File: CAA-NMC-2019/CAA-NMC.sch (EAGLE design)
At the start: 28 parts, among them IC1 ATTINY85-20SU, J1 M20-9980346

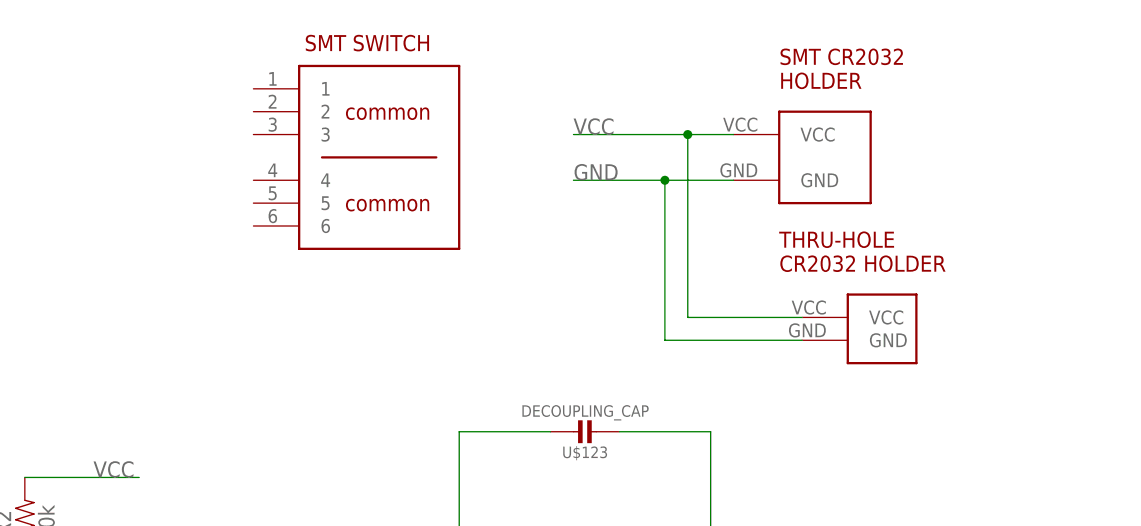
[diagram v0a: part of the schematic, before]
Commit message: fixed battery orientation
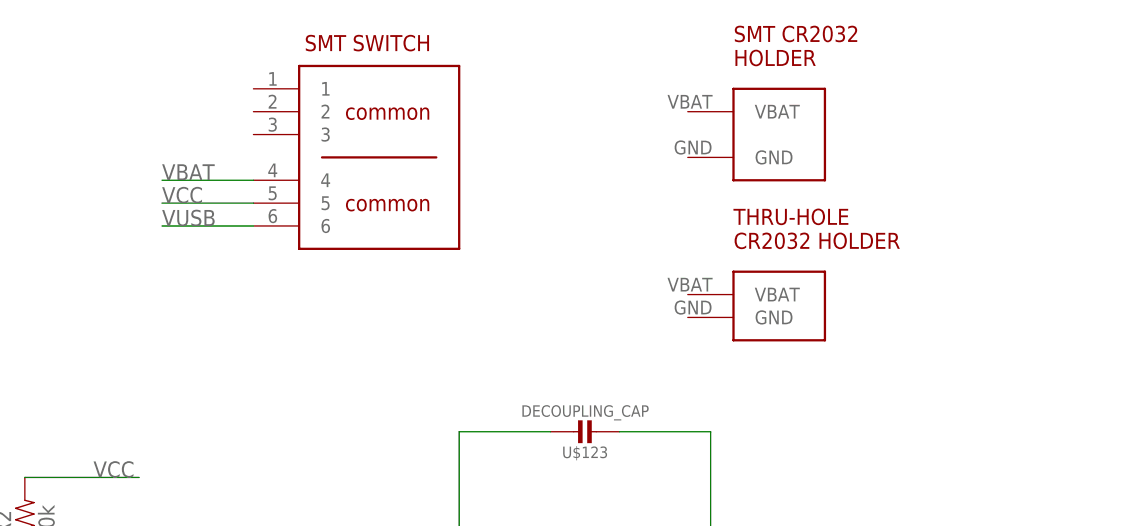
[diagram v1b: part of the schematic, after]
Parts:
- removed U$144: SMT-BATTERY-HOLDER, BadgeParts:SMT-BATTERY-HOLDER
- added U$3: THRU-CR-HOLDER, BadgeParts:THRU-CR-HOLDER
- U$2: value THRU-CR-HOLDER -> SMT-BATTERY-HOLDER; device BadgeParts:THRU-CR-HOLDER -> BadgeParts:SMT-BATTERY-HOLDER
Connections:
- new net VBAT: U$145.4
- new net VUSB: U$145.6
- net GND: no longer U$144.GND, U$2.GND
- net VCC: now also U$145.5; no longer U$144.VCC, U$2.VCC
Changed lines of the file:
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@@
 <part name="U$126" library="BadgeParts" deviceset="RESISTOR" device=""/>
 <part name="U$127" library="BadgeParts" deviceset="RESISTOR" device=""/>
-<part name="U$144" library="BadgeParts" deviceset="SMT-BATTERY-HOLDER" device=""/>
 <part name="U$145" library="BadgeParts" deviceset="SMT-SWITCH" device=""/>
 <part name="U$1" library="BadgeParts" deviceset="PROTO" device=""/>
-<part name="U$2" library="BadgeParts" deviceset="THRU-CR-HOLDER" device=""/>
 <part name="LED1" library="SparkFun-LED" library_urn="urn:adsk.eagle:library:529" deviceset="WS2812B" device="" package3d_urn="urn:adsk.eagle:package:39369/1" value="WS2812B"/>
 <part name="SUPPLY5" library="SparkFun-PowerSymbols" library_urn="urn:adsk.eagle:library:530" deviceset="VDD" device=""/>
@@
 <part name="R1" library="SparkFun-Resistors" library_urn="urn:adsk.eagle:library:532" deviceset="470OHM" device="-0603-1/10W-1%" package3d_urn="urn:adsk.eagle:package:39650/1" value="470"/>
 <part name="R2" library="SparkFun-Resistors" library_urn="urn:adsk.eagle:library:532" deviceset="10KOHM" device="-0603-1/10W-1%" package3d_urn="urn:adsk.eagle:package:39650/1" value="10k"/>
+<part name="U$2" library="BadgeParts" deviceset="SMT-BATTERY-HOLDER" device=""/>
+<part name="U$3" library="BadgeParts" deviceset="THRU-CR-HOLDER" device=""/>
 </parts>
 <sheets>
@@
 <attribute name="VALUE" x="-147.32" y="61.976" size="1.778" layer="96" font="vector" align="top-center"/>
 </instance>
-<instance part="U$144" gate="G$1" x="-127" y="124.46" smashed="yes"/>
 <instance part="U$145" gate="G$1" x="-180.34" y="129.54" smashed="yes"/>
 <instance part="U$1" gate="G$1" x="-63.5" y="101.6" smashed="yes"/>
-<instance part="U$2" gate="G$1" x="-119.38" y="104.14" smashed="yes"/>
 <instance part="LED1" gate="G$1" x="-284.48" y="116.84" smashed="yes">
 <attribute name="NAME" x="-297.18" y="125.222" size="1.778" layer="95"/>
@@
 <attribute name="VALUE" x="-209.296" y="81.28" size="1.778" layer="96" font="vector" rot="R90" align="top-center"/>
 </instance>
+<instance part="U$2" gate="G$1" x="-132.08" y="127" smashed="yes"/>
+<instance part="U$3" gate="G$1" x="-132.08" y="106.68" smashed="yes"/>
 </instances>
 <busses>
@@
 </segment>
 <segment>
-<pinref part="U$144" gate="G$1" pin="VCC"/>
-<wire x1="-132.08" y1="124.46" x2="-137.16" y2="124.46" width="0.1524" layer="91"/>
-<label x="-149.86" y="124.46" size="1.778" layer="95"/>
-<pinref part="U$2" gate="G$1" pin="VCC"/>
-<wire x1="-137.16" y1="124.46" x2="-149.86" y2="124.46" width="0.1524" layer="91"/>
-<wire x1="-124.46" y1="104.14" x2="-137.16" y2="104.14" width="0.1524" layer="91"/>
-<wire x1="-137.16" y1="104.14" x2="-137.16" y2="124.46" width="0.1524" layer="91"/>
-<junction x="-137.16" y="124.46"/>
-</segment>
-<segment>
 <pinref part="U$1" gate="G$1" pin="VCC"/>
 <wire x1="-68.58" y1="101.6" x2="-86.36" y2="101.6" width="0.1524" layer="91"/>
@@
 <wire x1="-210.82" y1="86.36" x2="-198.12" y2="86.36" width="0.1524" layer="91"/>
 <label x="-203.2" y="86.36" size="1.778" layer="95"/>
+</segment>
+<segment>
+<wire x1="-185.42" y1="116.84" x2="-195.58" y2="116.84" width="0.1524" layer="91"/>
+<pinref part="U$145" gate="G$1" pin="5"/>
+<label x="-195.58" y="116.84" size="1.778" layer="95"/>
 </segment>
 </net>
@@
 <wire x1="-5.08" y1="33.02" x2="-5.08" y2="40.64" width="0.1524" layer="91"/>
 <label x="-7.62" y="40.64" size="1.778" layer="95"/>
-</segment>
-<segment>
-<pinref part="U$144" gate="G$1" pin="GND"/>
-<wire x1="-132.08" y1="119.38" x2="-139.7" y2="119.38" width="0.1524" layer="91"/>
-<label x="-149.86" y="119.38" size="1.778" layer="95"/>
-<pinref part="U$2" gate="G$1" pin="GND"/>
-<wire x1="-139.7" y1="119.38" x2="-149.86" y2="119.38" width="0.1524" layer="91"/>
-<wire x1="-124.46" y1="101.6" x2="-139.7" y2="101.6" width="0.1524" layer="91"/>
-<wire x1="-139.7" y1="101.6" x2="-139.7" y2="119.38" width="0.1524" layer="91"/>
-<junction x="-139.7" y="119.38"/>
 </segment>
 <segment>
@@
 </segment>
 </net>
+<net name="VBAT" class="0">
+<segment>
+<wire x1="-185.42" y1="119.38" x2="-195.58" y2="119.38" width="0.1524" layer="91"/>
+<pinref part="U$145" gate="G$1" pin="4"/>
+<label x="-195.58" y="119.38" size="1.778" layer="95"/>
+</segment>
+</net>
+<net name="VUSB" class="0">
+<segment>
+<wire x1="-185.42" y1="114.3" x2="-195.58" y2="114.3" width="0.1524" layer="91"/>
+<pinref part="U$145" gate="G$1" pin="6"/>
+<label x="-195.58" y="114.3" size="1.778" layer="95"/>
+</segment>
+</net>

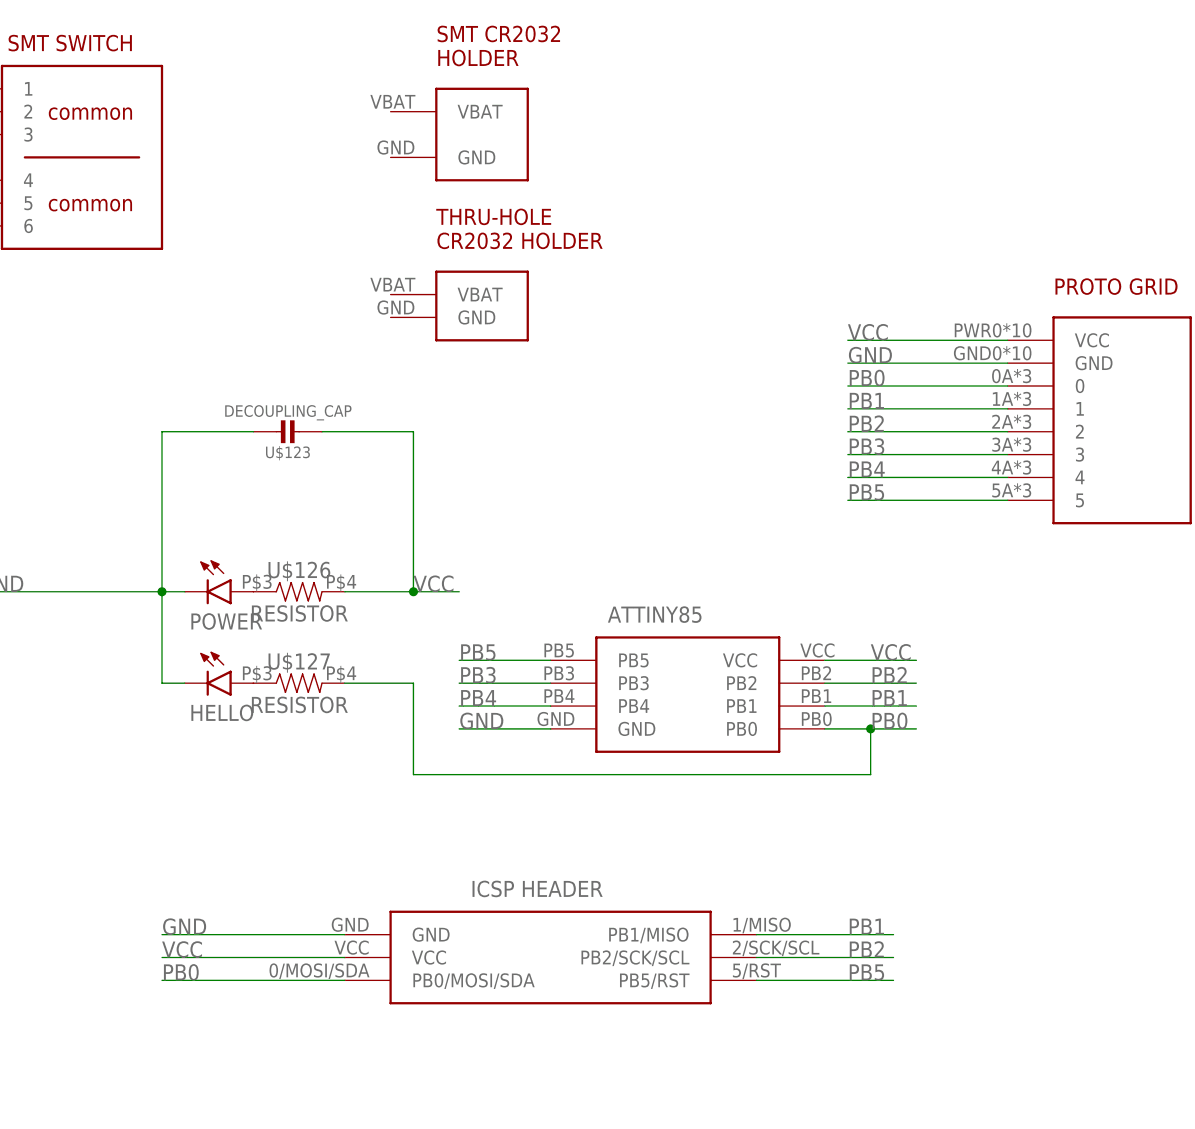
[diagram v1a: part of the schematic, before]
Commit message: Isolated battery/USB power supplies at switch
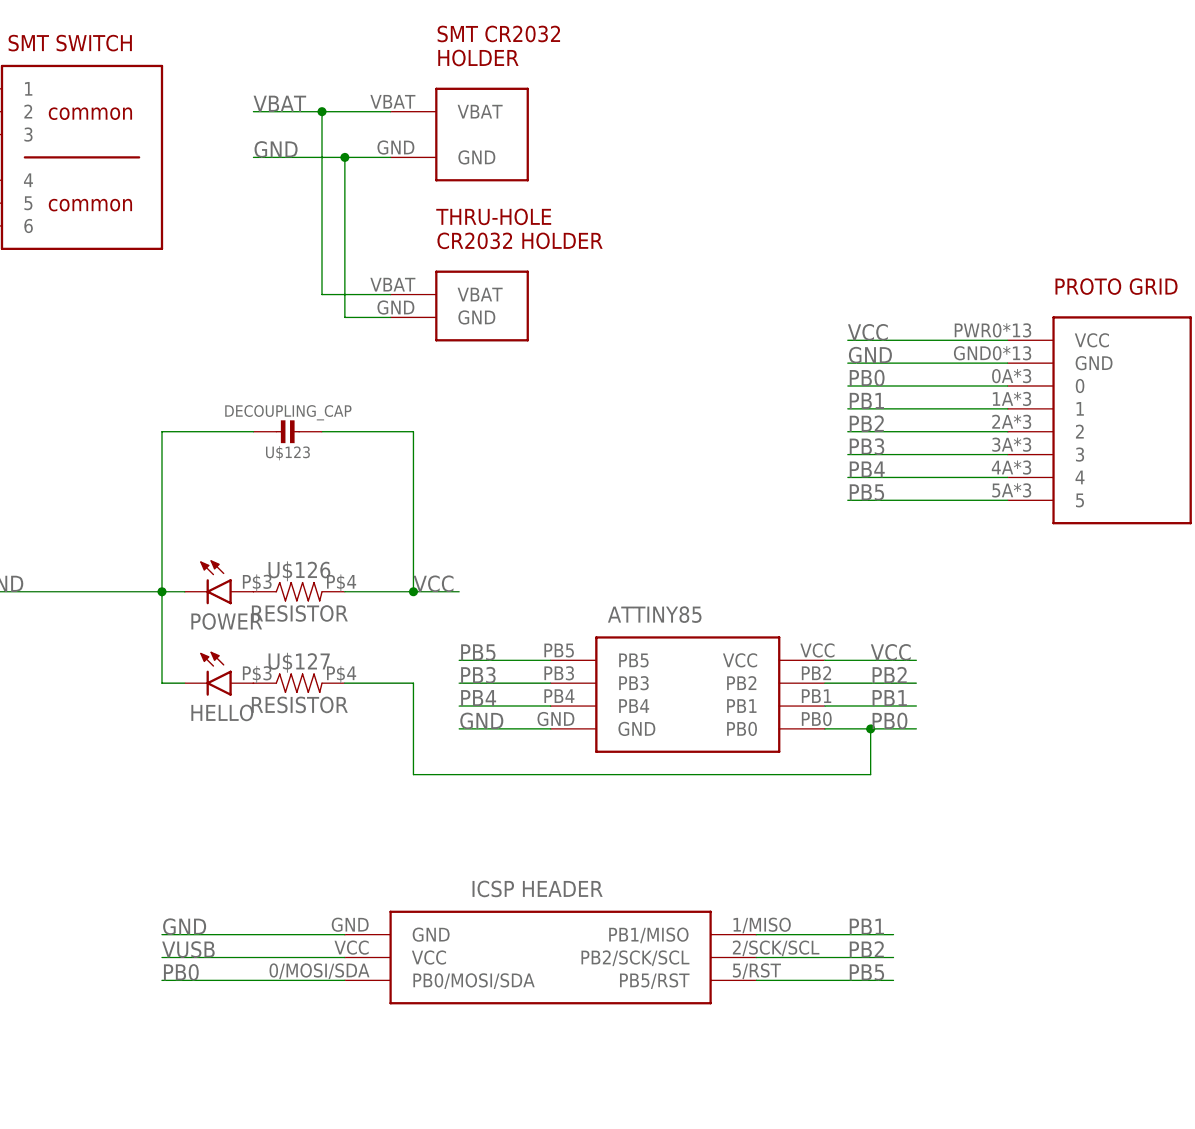
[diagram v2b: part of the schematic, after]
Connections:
- net GND: now also U$2.GND, U$3.GND
- net VBAT: now also U$2.VBAT, U$3.VBAT
- net VCC: no longer J1.VCC
- net VUSB: now also J1.VCC
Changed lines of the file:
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@@
-</segment>
-<segment>
-<pinref part="J1" gate="G$1" pin="VCC"/>
-<wire x1="-142.24" y1="33.02" x2="-162.56" y2="33.02" width="0.1524" layer="91"/>
-<label x="-162.56" y="33.02" size="1.778" layer="95"/>
 </segment>
 <segment>
@@
 <wire x1="-251.46" y1="27.94" x2="-251.46" y2="12.7" width="0.1524" layer="91"/>
 <junction x="-251.46" y="12.7"/>
+</segment>
+<segment>
+<pinref part="U$2" gate="G$1" pin="GND"/>
+<wire x1="-137.16" y1="121.92" x2="-142.24" y2="121.92" width="0.1524" layer="91"/>
+<wire x1="-142.24" y1="121.92" x2="-142.24" y2="104.14" width="0.1524" layer="91"/>
+<pinref part="U$3" gate="G$1" pin="GND"/>
+<wire x1="-142.24" y1="104.14" x2="-137.16" y2="104.14" width="0.1524" layer="91"/>
+<wire x1="-142.24" y1="121.92" x2="-152.4" y2="121.92" width="0.1524" layer="91"/>
+<junction x="-142.24" y="121.92"/>
+<label x="-152.4" y="121.92" size="1.778" layer="95"/>
 </segment>
 </net>
@@
 <label x="-195.58" y="119.38" size="1.778" layer="95"/>
 </segment>
+<segment>
+<pinref part="U$3" gate="G$1" pin="VBAT"/>
+<wire x1="-137.16" y1="106.68" x2="-144.78" y2="106.68" width="0.1524" layer="91"/>
+<wire x1="-144.78" y1="106.68" x2="-144.78" y2="127" width="0.1524" layer="91"/>
+<pinref part="U$2" gate="G$1" pin="VBAT"/>
+<wire x1="-144.78" y1="127" x2="-137.16" y2="127" width="0.1524" layer="91"/>
+<wire x1="-144.78" y1="127" x2="-152.4" y2="127" width="0.1524" layer="91"/>
+<junction x="-144.78" y="127"/>
+<label x="-152.4" y="127" size="1.778" layer="95"/>
+</segment>
 </net>
 <net name="VUSB" class="0">
@@
 <label x="-195.58" y="114.3" size="1.778" layer="95"/>
 </segment>
-</net>
+<segment>
+<pinref part="J1" gate="G$1" pin="VCC"/>
+<wire x1="-142.24" y1="33.02" x2="-162.56" y2="33.02" width="0.1524" layer="91"/>
+<label x="-162.56" y="33.02" size="1.778" layer="95"/>
+</segment>
+</net>

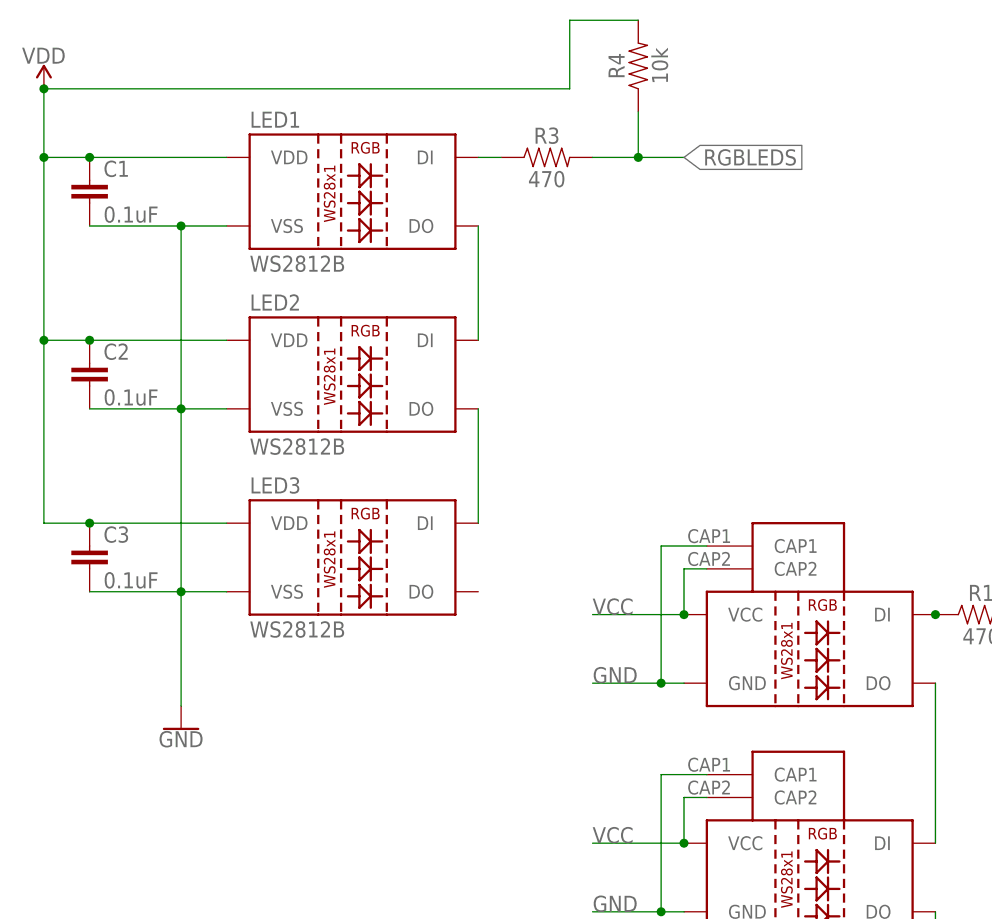
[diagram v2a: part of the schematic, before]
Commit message: restored most parts to layout
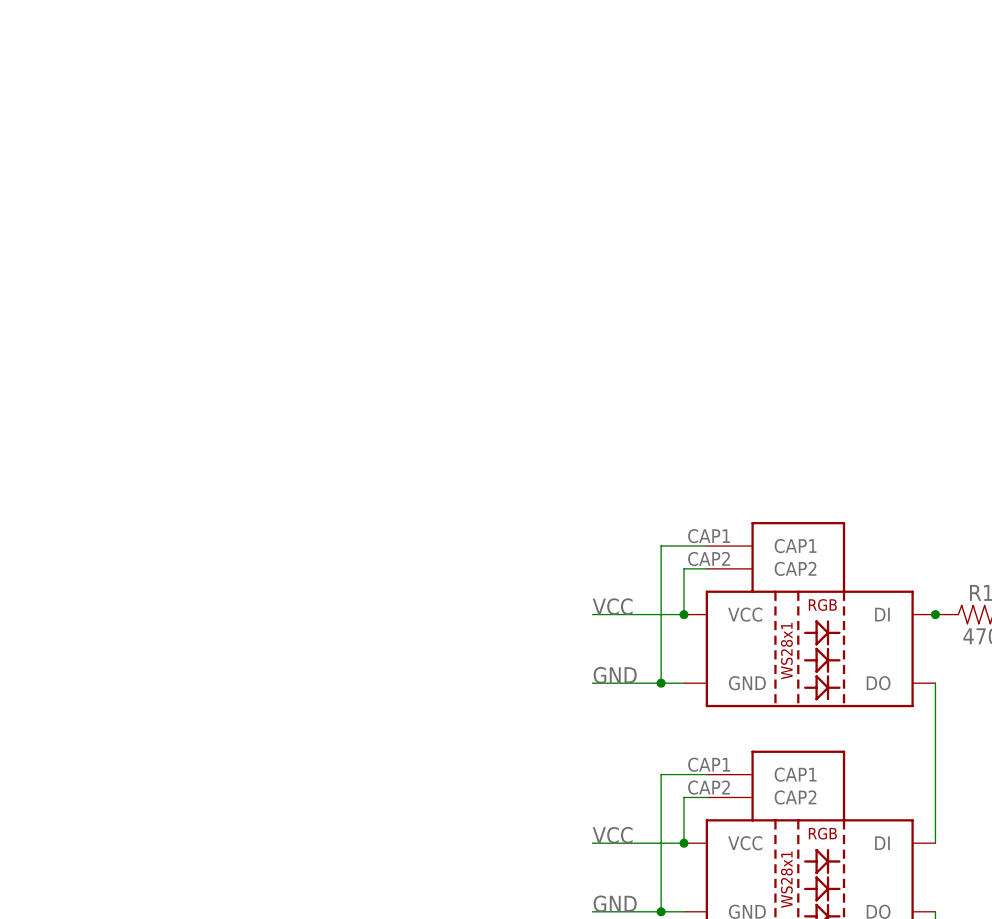
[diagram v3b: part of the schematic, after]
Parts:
- removed C1, C2, C3: 0.1uF, SparkFun-Capacitors:0.1UF-0603-25V-5%
- removed LED1, LED2, LED3: WS2812B, SparkFun-LED:WS2812B
- removed R3: 470, SparkFun-Resistors:470OHM-0603-1/10W-1%
- removed R4: 10k, SparkFun-Resistors:10KOHM-0603-1/10W-1%
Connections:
- removed net N$10: LED2.DO, LED3.DI
- removed net N$12: LED1.DI, R3.1
- removed net N$9: LED1.DO, LED2.DI
- removed net RGBLEDS: R3.2, R4.1
- removed net VDD: C1.1, C2.1, C3.1, LED1.VDD, LED2.VDD, LED3.VDD, R4.2
- net GND: no longer C1.2, C2.2, C3.2, LED1.VSS, LED2.VSS, LED3.VSS
